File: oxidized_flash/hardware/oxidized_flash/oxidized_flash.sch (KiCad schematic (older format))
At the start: 37 parts, among them J1 USB_A, J2 Conn_ARM_JTAG_SWD_10, U1 LM1117-3.3, U2 ATSAMD51G18A-MU, U3 IS21ES

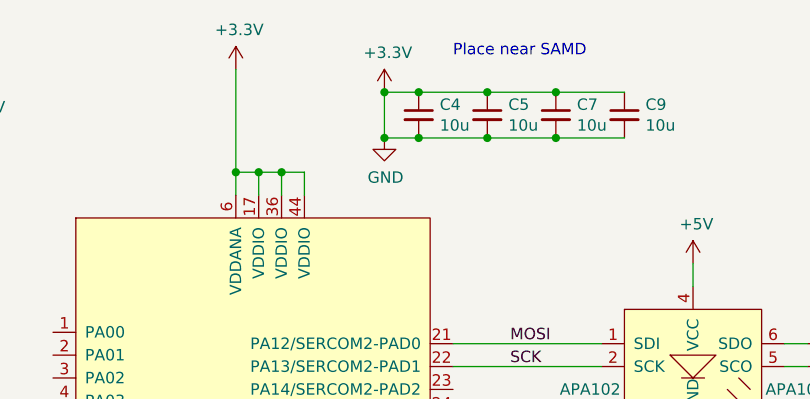
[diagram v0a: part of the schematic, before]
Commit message: Don't tie 3.3v directly to GND
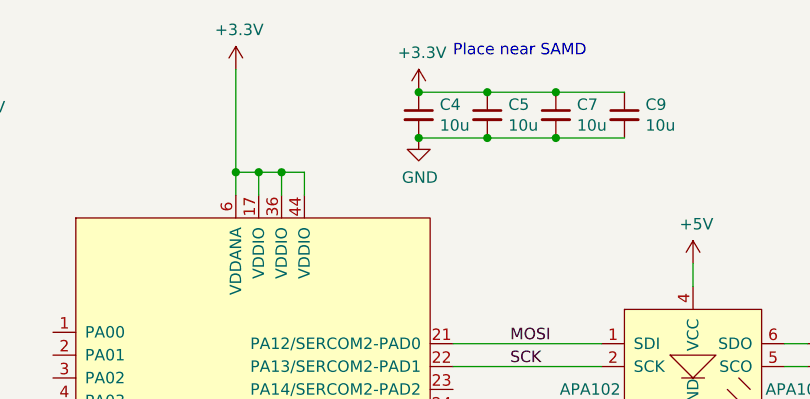
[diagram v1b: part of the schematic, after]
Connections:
- net +3V3: no longer C10.2, C11.2, C12.2, C13.2, C14.2, C15.2, C16.2, C17.2, C18.2, C19.2, C3.2, C4.2, C5.2, C6.2, C7.2, C8.2, C9.2, D2.3 (GND), D3.3 (GND), J1.4 (GND), J1.5 (Shield), J2.3 (GND), J2.5 (GND), J2.9 (GNDDetect), R1.2, R8.2, U1.1 (GND), U2.18 (GND), U2.35 (GND), U2.42 (GND), U2.5 (GND), U3.C4 (VSSQ), U3.E7 (VSS), U3.G5 (VSS), U3.H10 (VSS), U3.J5 (VSS), U3.K8 (VSS), U3.N2 (VSSQ), U3.N5 (VSSQ), U3.P4 (VSSQ), U3.P6 (VSSQ)
- new net GND: C10.2, C11.2, C12.2, C13.2, C14.2, C15.2, C16.2, C17.2, C18.2, C19.2, C3.2, C4.2, C5.2, C6.2, C7.2, C8.2, C9.2, D2.3 (GND), D3.3 (GND), J1.4 (GND), J1.5 (Shield), J2.3 (GND), J2.5 (GND), J2.9 (GNDDetect), R1.2, R8.2, U1.1 (GND), U2.18 (GND), U2.35 (GND), U2.42 (GND), U2.5 (GND), U3.C4 (VSSQ), U3.E7 (VSS), U3.G5 (VSS), U3.H10 (VSS), U3.J5 (VSS), U3.K8 (VSS), U3.N2 (VSSQ), U3.N5 (VSSQ), U3.P4 (VSSQ), U3.P6 (VSSQ)
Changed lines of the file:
@@
 	1    0    0    -1
 $EndComp
-Wire Wire Line
-	1600 3000 1600 3050
 $Comp
 L power:GND #PWR04
@@
 	1    0    0    -1
 $EndComp
-Wire Wire Line
-	1500 3000 1500 3050
-Wire Wire Line
-	1500 3050 1600 3050
-Connection ~ 1600 3050
-Wire Wire Line
-	1600 3050 1600 3100
 $Comp
 L Regulator_Linear:LM1117-3.3 U1
@@
 	3750 5050 3650 5050
 Connection ~ 3650 5050
-Wire Wire Line
-	4100 1150 4100 1350
 $Comp
 L power:+3.3V #PWR012
 U 1 1 5C460A45
-P 4100 1150
-F 0 "#PWR012" H 4100 1000 50  0001 C CNN
-F 1 "+3.3V" H 4115 1323 50  0000 C CNN
-F 2 "" H 4100 1150 50  0001 C CNN
-F 3 "" H 4100 1150 50  0001 C CNN
-	1    4100 1150
-	1    0    0    -1
-$EndComp
-$Comp
-L power:GND #PWR013
-U 1 1 5C460DD5
-P 4100 1350
-F 0 "#PWR013" H 4100 1100 50  0001 C CNN
-F 1 "GND" H 4105 1177 50  0000 C CNN
-F 2 "" H 4100 1350 50  0001 C CNN
-F 3 "" H 4100 1350 50  0001 C CNN
-	1    4100 1350
+P 4250 1150
+F 0 "#PWR012" H 4250 1000 50  0001 C CNN
+F 1 "+3.3V" H 4265 1323 50  0000 C CNN
+F 2 "" H 4250 1150 50  0001 C CNN
+F 3 "" H 4250 1150 50  0001 C CNN
+	1    4250 1150
 	1    0    0    -1
 $EndComp
@@
 	1    0    0    -1
 $EndComp
-Wire Wire Line
-	4250 1150 4100 1150
-Connection ~ 4100 1150
-Wire Wire Line
-	4250 1350 4100 1350
-Connection ~ 4100 1350
 $Comp
 L Device:C_Small C5
@@
 	4550 1350 4250 1350
 Connection ~ 4550 1350
-Connection ~ 4250 1350
 $Comp
 L ATSAMD:ATSAMD51G18A-MU U2
@@
 	1    0    0    -1
 $EndComp
+Wire Wire Line
+	1600 3000 1600 3050
+Wire Wire Line
+	1500 3000 1500 3050
+Wire Wire Line
+	1500 3050 1600 3050
+Connection ~ 1600 3050
+Wire Wire Line
+	1600 3050 1600 3100
+$Comp
+L power:GND #PWR?
+U 1 1 5C829A14
+P 4250 1350
+F 0 "#PWR?" H 4250 1100 50  0001 C CNN
+F 1 "GND" H 4255 1177 50  0000 C CNN
+F 2 "" H 4250 1350 50  0001 C CNN
+F 3 "" H 4250 1350 50  0001 C CNN
+	1    4250 1350
+	1    0    0    -1
+$EndComp
+Connection ~ 4250 1350
 $EndSCHEMATC

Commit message: Get passives close to their counterparts
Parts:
- C10, C11, C3, C4, C5, C6, C7, C8, C9: footprint Capacitor_SMD:C_0805_2012Metric -> Capacitor_SMD:C_0603_1608Metric
- C12, C13, C14, C15, C16, C17, C18, C19: footprint Capacitor_SMD:C_0805_2012Metric -> Capacitor_SMD:C_0603_1608Metric_Pad1.05x0.95mm_HandSolder
- D1, D4: footprint LED_SMD:LED_0805_2012Metric -> LED_SMD:LED_0603_1608Metric
- F1: footprint Fuse:Fuse_0805_2012Metric -> Fuse:Fuse_0603_1608Metric
- L1: footprint Inductor_SMD:L_0805_2012Metric -> Inductor_SMD:L_0603_1608Metric
- R1, R2, R3, R4, R5: footprint Resistor_SMD:R_0805_2012Metric -> Resistor_SMD:R_0603_1608Metric
- R6, R7, R8, R9: footprint Resistor_SMD:R_0805_2012Metric -> Resistor_SMD:R_0603_1608Metric_Pad1.05x0.95mm_HandSolder
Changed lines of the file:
@@
 F 0 "R3" H 4550 3450 50  0000 L CNN
 F 1 "10K" H 4550 3350 50  0000 L CNN
-F 2 "Resistor_SMD:R_0805_2012Metric" H 4500 3400 50  0001 C CNN
+F 2 "Resistor_SMD:R_0603_1608Metric" H 4500 3400 50  0001 C CNN
 F 3 "~" H 4500 3400 50  0001 C CNN
 	1    4500 3400
@@
 F 0 "R4" H 4800 3450 50  0000 L CNN
 F 1 "10K" H 4800 3350 50  0000 L CNN
-F 2 "Resistor_SMD:R_0805_2012Metric" H 4750 3400 50  0001 C CNN
+F 2 "Resistor_SMD:R_0603_1608Metric" H 4750 3400 50  0001 C CNN
 F 3 "~" H 4750 3400 50  0001 C CNN
 	1    4750 3400
@@
 F 0 "R5" H 5050 3450 50  0000 L CNN
 F 1 "10K" H 5050 3350 50  0000 L CNN
-F 2 "Resistor_SMD:R_0805_2012Metric" H 5000 3400 50  0001 C CNN
+F 2 "Resistor_SMD:R_0603_1608Metric" H 5000 3400 50  0001 C CNN
 F 3 "~" H 5000 3400 50  0001 C CNN
 	1    5000 3400
@@
 F 0 "R7" H 5300 3450 50  0000 L CNN
 F 1 "10K" H 5300 3350 50  0000 L CNN
-F 2 "Resistor_SMD:R_0805_2012Metric" H 5250 3400 50  0001 C CNN
+F 2 "Resistor_SMD:R_0603_1608Metric_Pad1.05x0.95mm_HandSolder" H 5250 3400 50  0001 C CNN
 F 3 "~" H 5250 3400 50  0001 C CNN
 	1    5250 3400
@@
 F 0 "R6" H 5059 4346 50  0000 L CNN
 F 1 "10K" H 5059 4255 50  0000 L CNN
-F 2 "Resistor_SMD:R_0805_2012Metric" H 5000 4300 50  0001 C CNN
+F 2 "Resistor_SMD:R_0603_1608Metric_Pad1.05x0.95mm_HandSolder" H 5000 4300 50  0001 C CNN
 F 3 "~" H 5000 4300 50  0001 C CNN
 	1    5000 4300
@@
 F 0 "C10" H 5542 5096 50  0000 L CNN
 F 1 "3u" H 5542 5005 50  0000 L CNN
-F 2 "Capacitor_SMD:C_0805_2012Metric" H 5450 5050 50  0001 C CNN
+F 2 "Capacitor_SMD:C_0603_1608Metric" H 5450 5050 50  0001 C CNN
 F 3 "~" H 5450 5050 50  0001 C CNN
 	1    5450 5050
@@
 F 0 "C4" H 4342 1296 50  0000 L CNN
 F 1 "10u" H 4342 1205 50  0000 L CNN
-F 2 "Capacitor_SMD:C_0805_2012Metric" H 4250 1250 50  0001 C CNN
+F 2 "Capacitor_SMD:C_0603_1608Metric" H 4250 1250 50  0001 C CNN
 F 3 "~" H 4250 1250 50  0001 C CNN
 	1    4250 1250
@@
 F 0 "C5" H 4642 1296 50  0000 L CNN
 F 1 "10u" H 4642 1205 50  0000 L CNN
-F 2 "Capacitor_SMD:C_0805_2012Metric" H 4550 1250 50  0001 C CNN
+F 2 "Capacitor_SMD:C_0603_1608Metric" H 4550 1250 50  0001 C CNN
 F 3 "~" H 4550 1250 50  0001 C CNN
 	1    4550 1250
@@
 F 0 "C7" H 4942 1296 50  0000 L CNN
 F 1 "10u" H 4942 1205 50  0000 L CNN
-F 2 "Capacitor_SMD:C_0805_2012Metric" H 4850 1250 50  0001 C CNN
+F 2 "Capacitor_SMD:C_0603_1608Metric" H 4850 1250 50  0001 C CNN
 F 3 "~" H 4850 1250 50  0001 C CNN
 	1    4850 1250
@@
 F 0 "C9" H 5242 1296 50  0000 L CNN
 F 1 "10u" H 5242 1205 50  0000 L CNN
-F 2 "Capacitor_SMD:C_0805_2012Metric" H 5150 1250 50  0001 C CNN
+F 2 "Capacitor_SMD:C_0603_1608Metric" H 5150 1250 50  0001 C CNN
 F 3 "~" H 5150 1250 50  0001 C CNN
 	1    5150 1250
@@
 F 0 "C8" H 5192 4896 50  0000 L CNN
 F 1 "0.1u" H 5192 4805 50  0000 L CNN
-F 2 "Capacitor_SMD:C_0805_2012Metric" H 5100 4850 50  0001 C CNN
+F 2 "Capacitor_SMD:C_0603_1608Metric" H 5100 4850 50  0001 C CNN
 F 3 "~" H 5100 4850 50  0001 C CNN
 	1    5100 4850
@@
 F 0 "C6" H 4842 4896 50  0000 L CNN
 F 1 "4.7u" H 4842 4805 50  0000 L CNN
-F 2 "Capacitor_SMD:C_0805_2012Metric" H 4750 4850 50  0001 C CNN
+F 2 "Capacitor_SMD:C_0603_1608Metric" H 4750 4850 50  0001 C CNN
 F 3 "~" H 4750 4850 50  0001 C CNN
 	1    4750 4850
@@
 F 0 "C11" H 7692 3646 50  0000 L CNN
 F 1 "3u" H 7692 3555 50  0000 L CNN
-F 2 "Capacitor_SMD:C_0805_2012Metric" H 7600 3600 50  0001 C CNN
+F 2 "Capacitor_SMD:C_0603_1608Metric" H 7600 3600 50  0001 C CNN
 F 3 "~" H 7600 3600 50  0001 C CNN
 	1    7600 3600
@@
 F 0 "C12" H 7942 3646 50  0000 L CNN
 F 1 "3u" H 7942 3555 50  0000 L CNN
-F 2 "Capacitor_SMD:C_0805_2012Metric" H 7850 3600 50  0001 C CNN
+F 2 "Capacitor_SMD:C_0603_1608Metric_Pad1.05x0.95mm_HandSolder" H 7850 3600 50  0001 C CNN
 F 3 "~" H 7850 3600 50  0001 C CNN
 	1    7850 3600
@@
 F 0 "C13" H 8192 3646 50  0000 L CNN
 F 1 "3u" H 8192 3555 50  0000 L CNN
-F 2 "Capacitor_SMD:C_0805_2012Metric" H 8100 3600 50  0001 C CNN
+F 2 "Capacitor_SMD:C_0603_1608Metric_Pad1.05x0.95mm_HandSolder" H 8100 3600 50  0001 C CNN
 F 3 "~" H 8100 3600 50  0001 C CNN
 	1    8100 3600
@@
 F 0 "C14" H 8442 3646 50  0000 L CNN
 F 1 "3u" H 8442 3555 50  0000 L CNN
-F 2 "Capacitor_SMD:C_0805_2012Metric" H 8350 3600 50  0001 C CNN
+F 2 "Capacitor_SMD:C_0603_1608Metric_Pad1.05x0.95mm_HandSolder" H 8350 3600 50  0001 C CNN
 F 3 "~" H 8350 3600 50  0001 C CNN
 	1    8350 3600
@@
 F 0 "C15" H 8692 3646 50  0000 L CNN
 F 1 "3u" H 8692 3555 50  0000 L CNN
-F 2 "Capacitor_SMD:C_0805_2012Metric" H 8600 3600 50  0001 C CNN
+F 2 "Capacitor_SMD:C_0603_1608Metric_Pad1.05x0.95mm_HandSolder" H 8600 3600 50  0001 C CNN
 F 3 "~" H 8600 3600 50  0001 C CNN
 	1    8600 3600
@@
 F 0 "C16" H 8942 3646 50  0000 L CNN
 F 1 "3u" H 8942 3555 50  0000 L CNN
-F 2 "Capacitor_SMD:C_0805_2012Metric" H 8850 3600 50  0001 C CNN
+F 2 "Capacitor_SMD:C_0603_1608Metric_Pad1.05x0.95mm_HandSolder" H 8850 3600 50  0001 C CNN
 F 3 "~" H 8850 3600 50  0001 C CNN
 	1    8850 3600
@@
 F 0 "C17" H 9192 3646 50  0000 L CNN
 F 1 "3u" H 9192 3555 50  0000 L CNN
-F 2 "Capacitor_SMD:C_0805_2012Metric" H 9100 3600 50  0001 C CNN
+F 2 "Capacitor_SMD:C_0603_1608Metric_Pad1.05x0.95mm_HandSolder" H 9100 3600 50  0001 C CNN
 F 3 "~" H 9100 3600 50  0001 C CNN
 	1    9100 3600
@@
 F 0 "C18" H 9442 3646 50  0000 L CNN
 F 1 "3u" H 9442 3555 50  0000 L CNN
-F 2 "Capacitor_SMD:C_0805_2012Metric" H 9350 3600 50  0001 C CNN
+F 2 "Capacitor_SMD:C_0603_1608Metric_Pad1.05x0.95mm_HandSolder" H 9350 3600 50  0001 C CNN
 F 3 "~" H 9350 3600 50  0001 C CNN
 	1    9350 3600
@@
 F 0 "C19" H 9692 3646 50  0000 L CNN
 F 1 "3u" H 9692 3555 50  0000 L CNN
-F 2 "Capacitor_SMD:C_0805_2012Metric" H 9600 3600 50  0001 C CNN
+F 2 "Capacitor_SMD:C_0603_1608Metric_Pad1.05x0.95mm_HandSolder" H 9600 3600 50  0001 C CNN
 F 3 "~" H 9600 3600 50  0001 C CNN
 	1    9600 3600
@@
 F 0 "R2" H 2259 3096 50  0000 L CNN
 F 1 "1k" H 2259 3005 50  0000 L CNN
-F 2 "Resistor_SMD:R_0805_2012Metric" H 2200 3050 50  0001 C CNN
+F 2 "Resistor_SMD:R_0603_1608Metric" H 2200 3050 50  0001 C CNN
 F 3 "~" H 2200 3050 50  0001 C CNN
 	1    2200 3050
@@
 F 0 "C3" H 2292 3446 50  0000 L CNN
 F 1 "0.1u" H 2292 3355 50  0000 L CNN
-F 2 "Capacitor_SMD:C_0805_2012Metric" H 2200 3400 50  0001 C CNN
+F 2 "Capacitor_SMD:C_0603_1608Metric" H 2200 3400 50  0001 C CNN
 F 3 "~" H 2200 3400 50  0001 C CNN
 	1    2200 3400
@@
 F 0 "R1" H 1109 4496 50  0000 L CNN
 F 1 "1k" H 1109 4405 50  0000 L CNN
-F 2 "Resistor_SMD:R_0805_2012Metric" H 1050 4450 50  0001 C CNN
+F 2 "Resistor_SMD:R_0603_1608Metric" H 1050 4450 50  0001 C CNN
 F 3 "~" H 1050 4450 50  0001 C CNN
 	1    1050 4450
@@
 F 0 "D1" V 1096 4082 50  0000 R CNN
 F 1 "OK_Led" V 1005 4082 50  0000 R CNN
-F 2 "LED_SMD:LED_0805_2012Metric" V 1050 4150 50  0001 C CNN
+F 2 "LED_SMD:LED_0603_1608Metric" V 1050 4150 50  0001 C CNN
 F 3 "~" V 1050 4150 50  0001 C CNN
 	1    1050 4150
@@
 F 0 "F1" H 1150 1385 50  0000 C CNN
 F 1 "500mA" H 1150 1294 50  0000 C CNN
-F 2 "Fuse:Fuse_0805_2012Metric" H 1150 1200 50  0001 C CNN
+F 2 "Fuse:Fuse_0603_1608Metric" H 1150 1200 50  0001 C CNN
 F 3 "~" H 1150 1200 50  0001 C CNN
 	1    1150 1200
@@
 F 0 "L1" V 4350 4750 50  0000 C CNN
 F 1 "10uH" V 4450 4750 50  0000 C CNN
-F 2 "Inductor_SMD:L_0805_2012Metric" H 4550 4750 50  0001 C CNN
+F 2 "Inductor_SMD:L_0603_1608Metric" H 4550 4750 50  0001 C CNN
 F 3 "~" H 4550 4750 50  0001 C CNN
 	1    4550 4750
@@
 F 0 "R9" H 2459 3996 50  0000 L CNN
 F 1 "10k" H 2459 3905 50  0000 L CNN
-F 2 "Resistor_SMD:R_0805_2012Metric" H 2400 3950 50  0001 C CNN
+F 2 "Resistor_SMD:R_0603_1608Metric_Pad1.05x0.95mm_HandSolder" H 2400 3950 50  0001 C CNN
 F 3 "~" H 2400 3950 50  0001 C CNN
 	1    2400 3950
@@
 F 0 "D4" V 1596 4082 50  0000 R CNN
 F 1 "PWR_LED" V 1505 4082 50  0000 R CNN
-F 2 "LED_SMD:LED_0805_2012Metric" V 1550 4150 50  0001 C CNN
+F 2 "LED_SMD:LED_0603_1608Metric" V 1550 4150 50  0001 C CNN
 F 3 "~" V 1550 4150 50  0001 C CNN
 	1    1550 4150
@@
 F 0 "R8" H 1609 4496 50  0000 L CNN
 F 1 "1k" H 1609 4405 50  0000 L CNN
-F 2 "Resistor_SMD:R_0805_2012Metric" H 1550 4450 50  0001 C CNN
+F 2 "Resistor_SMD:R_0603_1608Metric_Pad1.05x0.95mm_HandSolder" H 1550 4450 50  0001 C CNN
 F 3 "~" H 1550 4450 50  0001 C CNN
 	1    1550 4450
@@
 	1600 3050 1600 3100
 $Comp
-L power:GND #PWR?
+L power:GND #PWR0106
 U 1 1 5C829A14
 P 4250 1350
-F 0 "#PWR?" H 4250 1100 50  0001 C CNN
+F 0 "#PWR0106" H 4250 1100 50  0001 C CNN
 F 1 "GND" H 4255 1177 50  0000 C CNN
 F 2 "" H 4250 1350 50  0001 C CNN

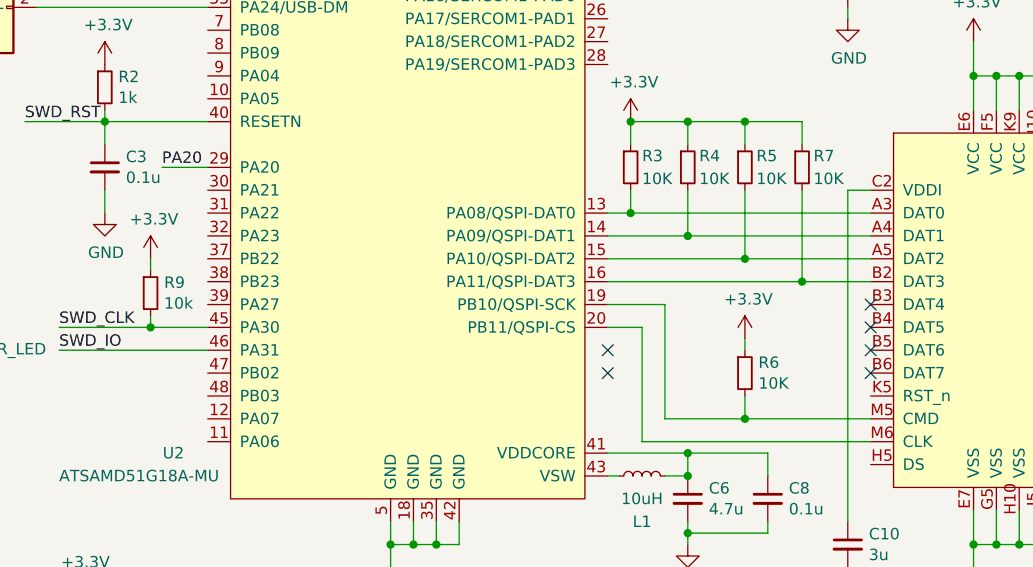
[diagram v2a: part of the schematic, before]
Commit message: Start initial track routing
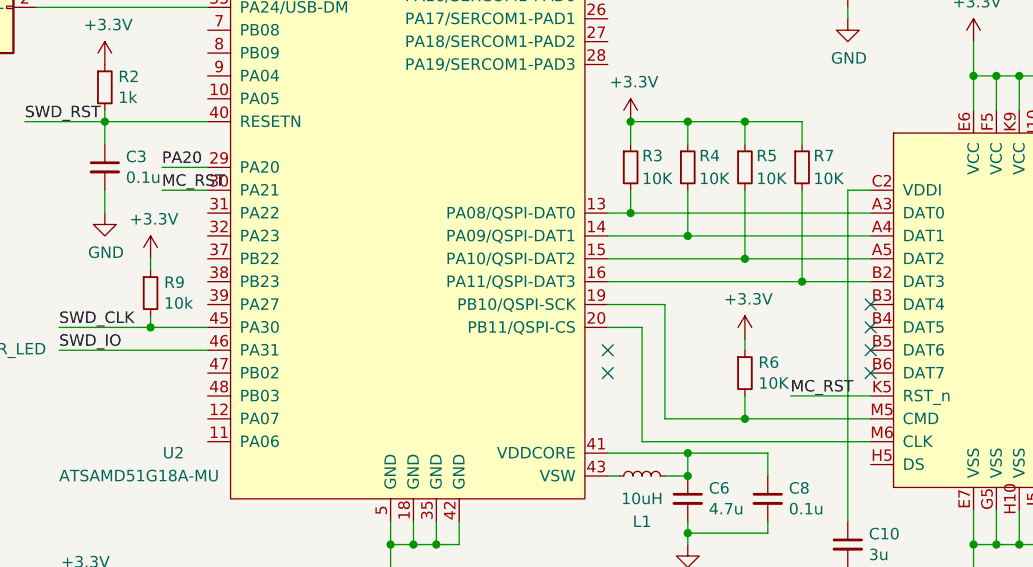
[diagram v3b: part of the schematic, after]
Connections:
- net MC_RST: now reaches U3.K5 (RST_n)
- net MC_RST: now also U2.30 (PA21)
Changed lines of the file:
@@
 $EndDescr
-$Comp
-L eMMC:IS21ES U3
-U 1 1 5C43BCCB
-P 6000 4100
-F 0 "U3" H 7228 4221 50  0000 L CNN
-F 1 "IS21ES" H 7228 4130 50  0000 L CNN
-F 2 "Custom_BGA:FBGA-153_14x14_11.5x13.0mm" H 6000 4100 50  0001 C CNN
-F 3 "" H 6000 4100 50  0001 C CNN
-	1    6000 4100
-	1    0    0    -1
-$EndComp
 $Comp
 L power:GND #PWR04
@@
 $EndComp
 Connection ~ 4250 1350
+$Comp
+L eMMC:IS21ES U3
+U 1 1 5C43BCCB
+P 6000 4100
+F 0 "U3" H 7228 4221 50  0000 L CNN
+F 1 "IS21ES" H 7228 4130 50  0000 L CNN
+F 2 "Custom_BGA:FBGA-153_14x14_11.5x13.0mm" H 6000 4100 50  0001 C CNN
+F 3 "" H 6000 4100 50  0001 C CNN
+	1    6000 4100
+	1    0    0    -1
+$EndComp
+Wire Wire Line
+	5550 4400 5200 4400
+Text Label 5200 4400 0    50   ~ 0
+MC_RST
+Wire Wire Line
+	2650 3500 2450 3500
+Text Label 2450 3500 0    50   ~ 0
+MC_RST
 $EndSCHEMATC

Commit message: More routing
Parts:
- D2, D3: symbol Custom_LED:APA102 -> oxidized_flash-rescue:APA102-Custom_LED
- J2: symbol Connector:Conn_ARM_JTAG_SWD_10 -> oxidized_flash-rescue:Conn_ARM_JTAG_SWD_10-Connector
- U2: symbol ATSAMD:ATSAMD51G18A-MU -> oxidized_flash-rescue:ATSAMD51G18A-MU-ATSAMD
- U3: symbol eMMC:IS21ES -> oxidized_flash-rescue:IS21ES-eMMC
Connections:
- net at R3.2, U3.A3 (DAT0): now also U2.14 (PA09/SDHC0-SDDAT0); no longer U2.13 (PA08/QSPI-DAT0)
- net at R4.2, U3.A4 (DAT1): now also U2.15 (PA10/SDHC0-SDDAT1); no longer U2.14 (PA09/QSPI-DAT1)
- net at R5.2, U3.A5 (DAT2): now also U2.16 (PA11/SDHC0-SDDAT2); no longer U2.15 (PA10/QSPI-DAT2)
- net at R7.2, U3.B2 (DAT3): now also U2.19 (PB10/SDHC0-SDDAT3); no longer U2.16 (PA11/QSPI-DAT3)
- net at R6.2, U3.M5 (CMD): now also U2.13 (PA08/SDHC0-SDCMD); no longer U2.19 (PB10/QSPI-SCK)
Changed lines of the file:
@@
 EESchema Schematic File Version 4
 LIBS:power
-LIBS:device
-LIBS:switches
-LIBS:relays
-LIBS:motors
-LIBS:transistors
-LIBS:conn
-LIBS:linear
-LIBS:regul
 LIBS:74xx
-LIBS:cmos4000
-LIBS:adc-dac
-LIBS:memory
-LIBS:xilinx
-LIBS:microcontrollers
-LIBS:dsp
-LIBS:microchip
-LIBS:analog_switches
-LIBS:motorola
-LIBS:texas
-LIBS:intel
-LIBS:audio
-LIBS:interface
-LIBS:digital-audio
-LIBS:philips
-LIBS:display
-LIBS:cypress
-LIBS:siliconi
-LIBS:opto
-LIBS:atmel
-LIBS:contrib
-LIBS:valves
 LIBS:oxidized_flash-cache
 EELAYER 29 0
@@
 Connection ~ 4550 1350
 $Comp
-L ATSAMD:ATSAMD51G18A-MU U2
+L oxidized_flash-rescue:ATSAMD51G18A-MU-ATSAMD U2
 U 1 1 5C4804F6
 P 3600 3350
@@
 Place near MMC card
 $Comp
-L Custom_LED:APA102 D2
+L oxidized_flash-rescue:APA102-Custom_LED D2
 U 1 1 5C5453FD
 P 5450 2350
@@
 	3450 1050 3450 1500
 $Comp
-L Custom_LED:APA102 D3
+L oxidized_flash-rescue:APA102-Custom_LED D3
 U 1 1 5C545A1F
 P 6350 2350
@@
 NoConn ~ 6750 2350
 $Comp
-L Connector:Conn_ARM_JTAG_SWD_10 J2
+L oxidized_flash-rescue:Conn_ARM_JTAG_SWD_10-Connector J2
 U 1 1 5C6F27D1
 P 2100 6000
@@
 Connection ~ 4250 1350
 $Comp
-L eMMC:IS21ES U3
+L oxidized_flash-rescue:IS21ES-eMMC U3
 U 1 1 5C43BCCB
 P 6000 4100
